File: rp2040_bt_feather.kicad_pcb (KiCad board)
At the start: 2 copper layers, 50.8 x 22.9 mm, 81 parts, among them J1 HRO TYPE-C-31-M-12, J2 LIPO_JSTPH, J3 Conn_01x16, J4 Conn_01x12, J5 Qwiic/STEMMA QT, J6 SWD, Q1 DMG3415U-7?, Q2 DMG3415U-7?, SW1 SW_Push, SW2 SW_Push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

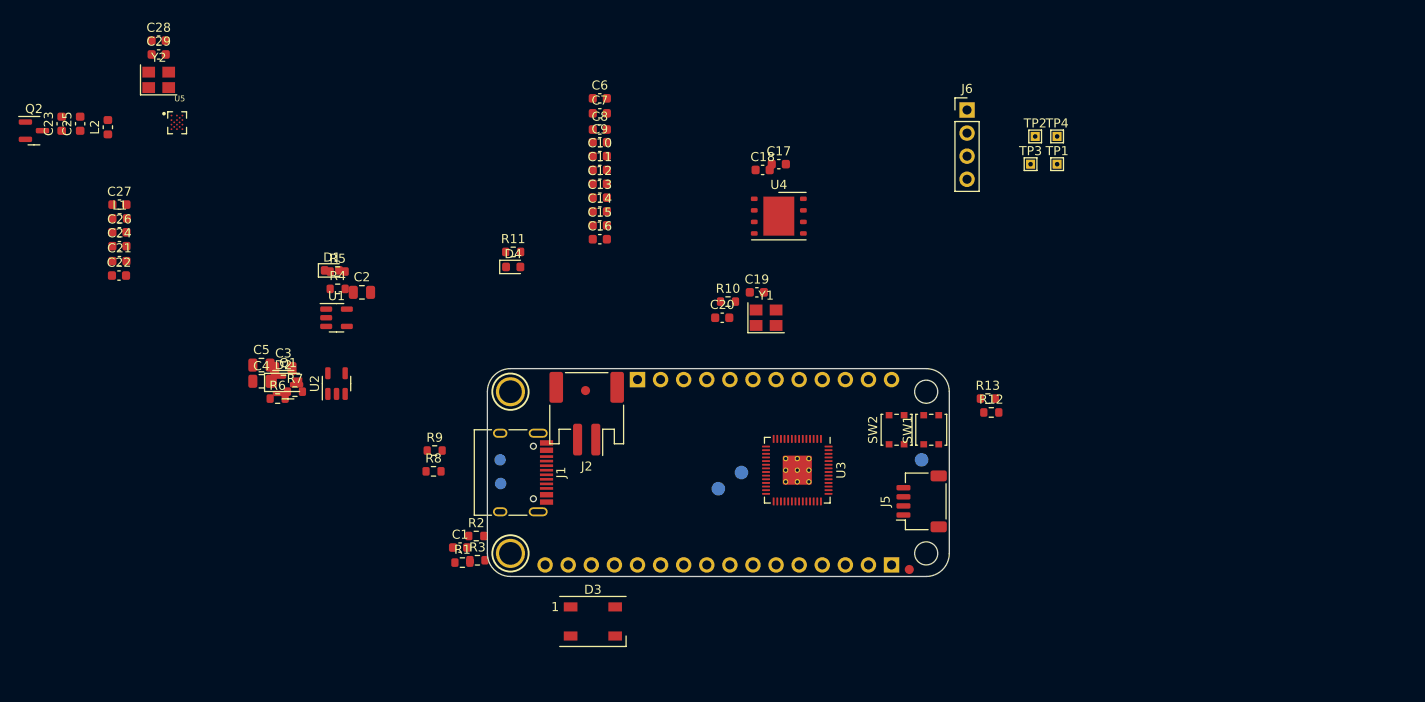
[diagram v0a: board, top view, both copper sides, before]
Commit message: Lay out power input and supporting passives
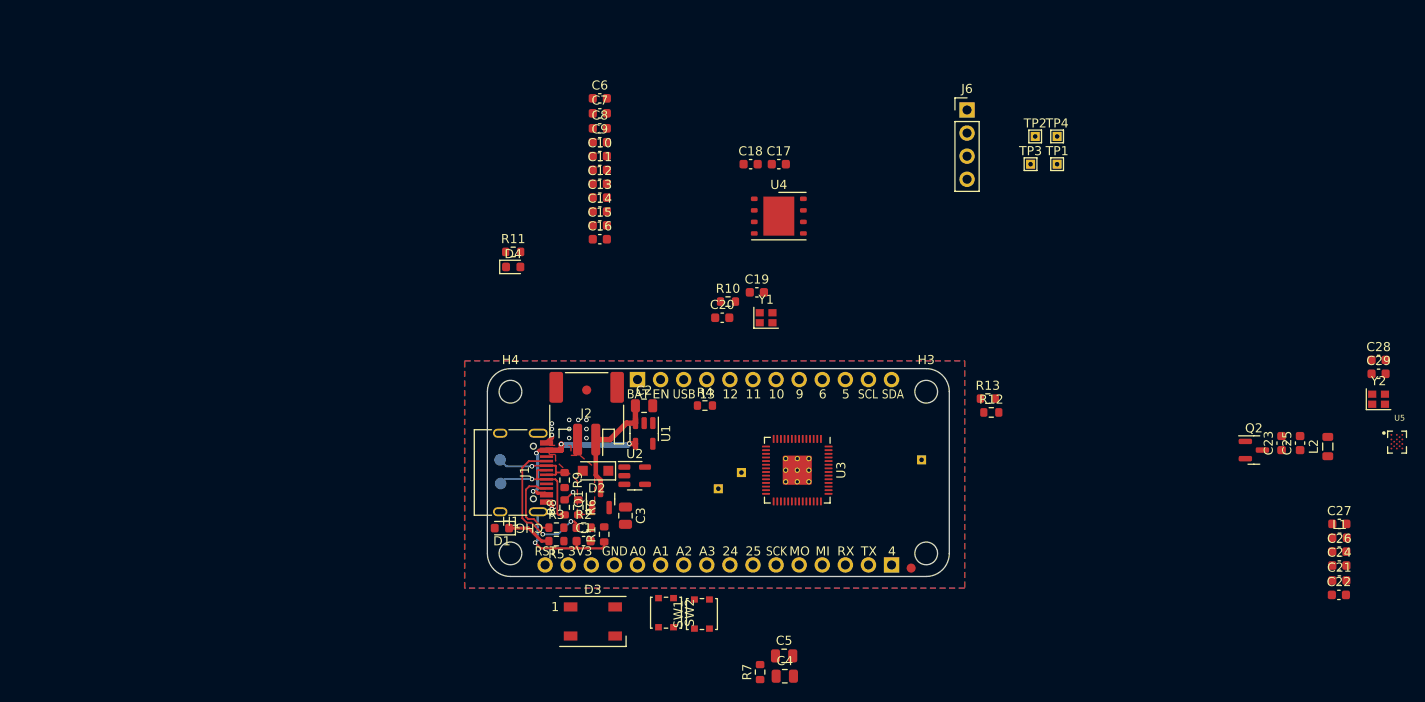
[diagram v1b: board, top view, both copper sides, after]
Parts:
- removed @HOLE0, @HOLE1: , 
- removed J5: Qwiic/STEMMA QT, Connector_JST:JST_SH_SM04B-SRSS-TB_1x04-1MP_P1.00mm_Horizontal
- removed U$31, U$32: MOUNTINGHOLE2.5, Adafruit Feather RP2040:MOUNTINGHOLE_2.5_PLATED
- removed U$34, U$35: FIDUCIAL_1MM, Adafruit Feather RP2040:FIDUCIAL_1MM
- removed U$43: , Adafruit Feather RP2040:RP2040_TOP
- added FID1: Fiducial, Fiducial:Fiducial_1mm_Mask2mm, F.Cu at (129.1, 107.8)
- added FID2: Fiducial, Fiducial:Fiducial_1mm_Mask2mm, F.Cu at (93.4, 88.2)
- added H1: MountingHole, MountingHole:MountingHole_2.5mm, F.Cu at (85.0, 106.2)
- added H2: MountingHole, MountingHole:MountingHole_2.5mm, F.Cu at (130.8, 106.2)
- added H3: MountingHole, MountingHole:MountingHole_2.5mm, F.Cu at (130.8, 88.4)
- added H4: MountingHole, MountingHole:MountingHole_2.5mm, F.Cu at (85.0, 88.4)
- L2: footprint Inductor_SMD:L_0603_1608Metric -> Inductor_SMD:L_0805_2012Metric
- TP1, TP3: value (none) -> SWDIO; footprint Adafruit Feather RP2040:TESTPOINT_ROUND_1.5MM_NO -> TestPoint:TestPoint_THTPad_1.0x1.0mm_Drill0.5mm
- TP2: value (none) -> SWCLK; footprint Adafruit Feather RP2040:TESTPOINT_ROUND_1.5MM_NO -> TestPoint:TestPoint_THTPad_1.0x1.0mm_Drill0.5mm
- Y1, Y2: footprint Crystal:Crystal_SMD_3225-4Pin_3.2x2.5mm -> Crystal:Crystal_SMD_2016-4Pin_2.0x1.6mm
- moved C23 138.7 mm to (169.8, 94.0)
- moved C21 138.7 mm to (176.2, 109.2)
- moved C22 138.7 mm to (176.1, 110.7)
- moved C24 138.7 mm to (176.2, 107.5)
- moved C25 138.7 mm to (171.9, 94.0)
- moved C26 138.7 mm to (176.2, 106.0)
- moved C27 138.7 mm to (176.2, 102.9)
- moved C28 138.7 mm to (180.5, 84.9)
- moved C29 138.7 mm to (180.5, 86.4)
- moved L1 138.7 mm to (176.2, 104.5)
- moved L2 138.7 mm to (174.9, 94.4)
- moved Q2 138.7 mm to (166.8, 94.8)
- moved U5 138.7 mm to (182.5, 93.9)
- moved Y2 138.7 mm to (180.5, 89.2)
- moved C4 66.1 mm to (115.2, 119.7)
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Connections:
- J2 pad 1: GND -> +BATT
- J2 pad 2: +BATT -> GND
- Q1 pad 1: +BATT -> VUSB
- Q1 pad 2: VUSB -> /V_IN
- Q1 pad 3: /V_IN -> +BATT
- Q2 pad 1: /DA_VIN -> /DA_PWR
- Q2 pad 2: /DA_PWR -> +3V3
- Q2 pad 3: +3V3 -> /DA_VIN
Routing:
- net VUSB: track 0.00 -> 17.8 mm, vias 0 -> 4
- net /CC1: track 0.00 -> 16.3 mm, vias 0 -> 2
- net /D+: track 0.00 -> 13.0 mm, vias 0 -> 1
- net +BATT: track 0.00 -> 12.9 mm
- net Net-(C1-Pad1): track 0.00 -> 12.9 mm, vias 0 -> 1
- net /D-: track 0.00 -> 9.29 mm, vias 0 -> 1
- net /CC2: track 0.00 -> 8.52 mm
- net Net-(D1-Pad1): track 0.00 -> 4.97 mm
- net GND: track 0.00 -> 2.27 mm, vias 0 -> 12
- net /RP_D+: track 0.00 -> 1.28 mm, vias 0 -> 1
- added copper zone on B.Cu, net GND
- added copper zone on F.Cu, net GND
- added copper zone on F.Cu, net VUSB
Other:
- board text added: "10"
- board text added: "11"
- board text added: "12"
- board text added: "13"
- board text added: "24"
- board text added: "25"
- board text added: "3V3"
- board text added: "4"
- board text added: "5"
- board text added: "6"
- board text added: "9"
- board text added: "A0"
- board text added: "A1"
- board text added: "A2"
- board text added: "A3"
- board text added: "BAT"
- board text added: "CHG"
- board text added: "EN"
- board text added: "GND"
- board text added: "MI"
- board text added: "MO"
- board text added: "RST"
- board text added: "RX"
- board text added: "SCK"
- board text added: "SCL"
- board text added: "SDA"
- board text added: "TX"
- board text added: "USB"
